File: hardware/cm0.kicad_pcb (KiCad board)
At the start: 4 copper layers, 85 x 56 mm, 252 parts, among them J1 USB_A_Stacked, J10 AudioJack_PJ-342, J2 USB_C_Receptacle_USB2.0_14P, J3 USB_C_Receptacle_USB2.0_14P, J4 USB_C_Receptacle_USB2.0_14P, J5 GPDI_A, J6 Micro_SD_Card_Det1, J7 RJ45_Hanrun_HR913550A_Horizon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, J8 Conn_01x03, J9 Conn_02x20_Odd_Even, Q1 BSN20, Q2 AO3415A, Q3 BSN20, Q4 BSN20, Q5 MMBT3904, U1 H3, U10 SY6280AAC, U11 SY6280AAC, U12 SY6280AAC, U13 TPD2EUSB30, U14 TPD2EUSB30, U15 TPD2EUSB30, U16 TPD2EUSB30, U17 HUSB237, U18 TPD2EUSB30, U19 UCL0524P, U2 H5TQ4G63EFR, U20 UCL0524P, U21 EMMC5.1_BGA153, U22 AP6212, U23 UCL0524P, U3 SY8088, U4 SY8088, U5 SY8088, U6 SY8089A, U7 SY8113, U8 SY8088, U9 SY6280AAC, Y1 32kHz, Y2 26MHz, Y3 24MHz

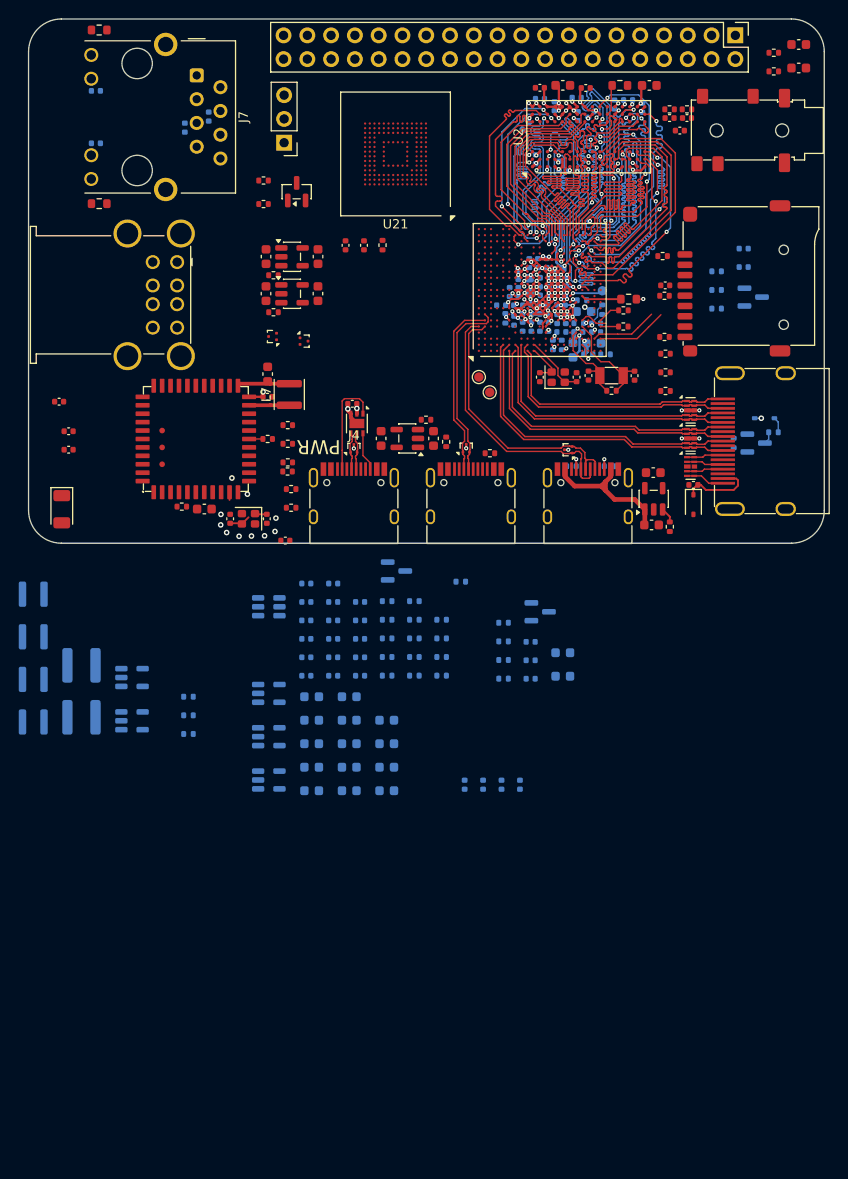
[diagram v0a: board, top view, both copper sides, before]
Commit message: Integrating DCDC converters
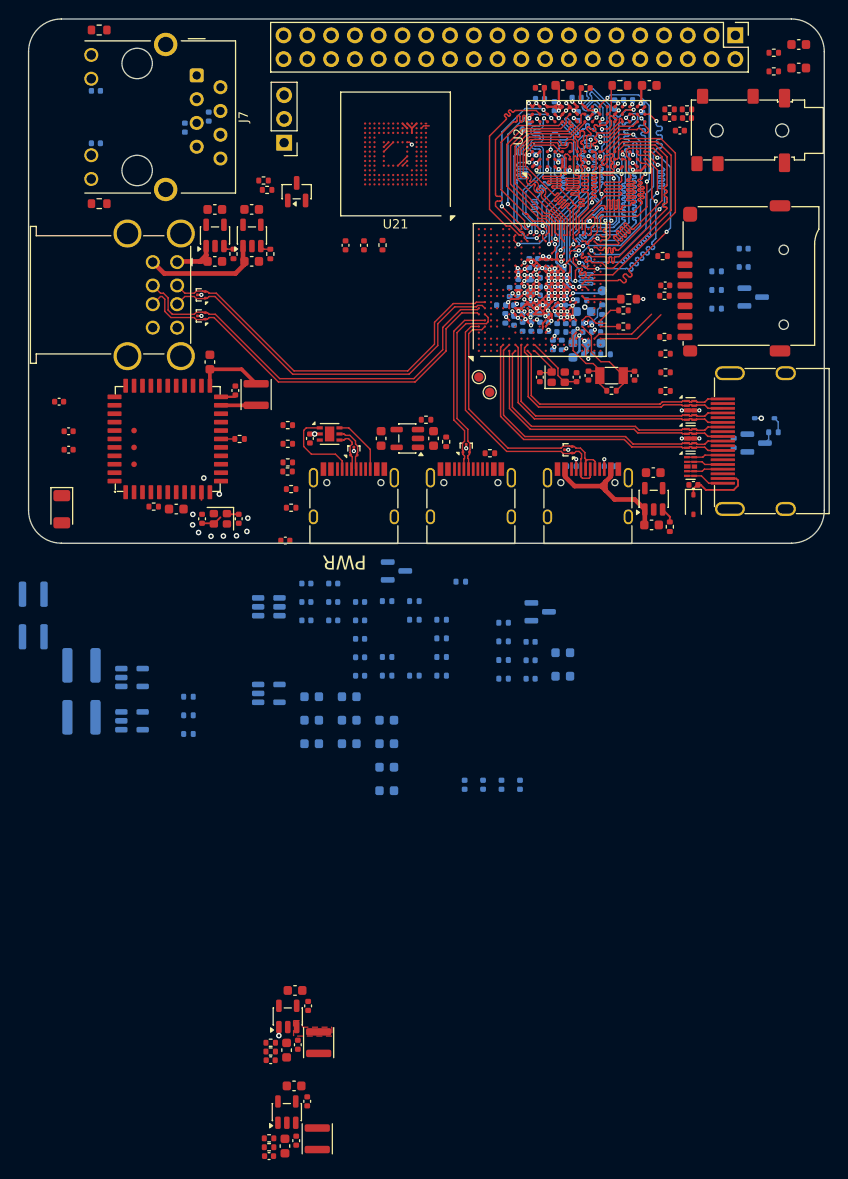
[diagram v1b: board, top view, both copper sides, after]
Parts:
- C59, C60, C61, C62, C63, C64, C65, C66, C67, C68, L1, L2, R12, R13, R14, R16, U3, U4: moved to F.Cu
- R22: value 30.1k -> 33k
- moved R13 55.6 mm to (88.2, 208.3), turned to 180 degrees
- moved R12 54.6 mm to (88.2, 209.2)
- moved L1 53.9 mm to (93.3, 208.3), turned to -90 degrees
- moved C62 53.7 mm to (91.1, 208.6), turned to -90 degrees
- moved C61 53.7 mm to (88.2, 210.2), turned to 180 degrees
- moved L2 49.3 mm to (93.5, 198.1), turned to -90 degrees
- moved R16 46.9 mm to (88.4, 198.1), turned to 180 degrees
- moved R14 45.9 mm to (88.4, 199.0)
- moved C60 45.5 mm to (92.3, 204.3), turned to 90 degrees
- moved C67 43.4 mm to (91.3, 198.3), turned to -90 degrees
- moved C66 43.2 mm to (88.4, 200.0), turned to 180 degrees
- moved C63 41.0 mm to (89.9, 209.1), turned to 90 degrees
- moved U3 40.1 mm to (90.1, 205.5), turned to 90 degrees
- moved C65 35.3 mm to (92.4, 194.2), turned to 90 degrees
- moved C59 32.1 mm to (90.9, 202.7), turned to 180 degrees
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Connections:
- J1 pad 2: /H3/USB_D2- -> /H3/USB_D3-
- J1 pad 3: /H3/USB_D2+ -> /H3/USB_D3+
- J1 pad 6: /H3/USB_D3- -> /H3/USB_D2-
- J1 pad 7: /H3/USB_D3+ -> /H3/USB_D2+
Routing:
- net /H3/USB_D2-: track 0.00 -> 44.4 mm
- net /H3/USB_D2+: track 0.00 -> 44.4 mm
- net /H3/USB_D3+: track 0.00 -> 41.4 mm
- net /H3/USB_D3-: track 0.00 -> 41.3 mm
- net /USB/USB_VBUS3: track 0.00 -> 12.7 mm
- net /USB/USB_VBUS2: track 0.00 -> 5.91 mm
- net +3V3: track 0.70 -> 4.03 mm
- net GND: track 98.3 -> 101.1 mm, vias 74 -> 75
- net /USB/PWR_CC2: track 4.15 -> 6.35 mm
- net /USB/PWR_CC1: track 11.0 -> 9.17 mm
- net Net-(U22-VIN_LDO): track 5.82 -> 7.34 mm
- net Net-(U10-ISET): track 0.00 -> 1.16 mm
- net Net-(U11-ISET): track 0.00 -> 1.16 mm
- net /USB/PWR_D-: track 4.11 -> 5.25 mm
- net /H3/PWR_DRAM: track 1.04 -> 1.95 mm, vias 0 -> 1
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- added copper zone on F.Cu, net Net-(U4-LX)
